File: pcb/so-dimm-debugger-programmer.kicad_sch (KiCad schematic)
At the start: 22 parts, among them J1 1612618-4, J12 Conn_01x06_Pin, J2 Conn_01x06_Pin, J3 Conn_01x04_Pin, J4 Conn_01x04_Pin, J8 Conn_02x16_Odd_Even, J9 Conn_01x04_Pin, SW1 SW_Push, SW2 SW_Push, U1 AP2112K-3.3

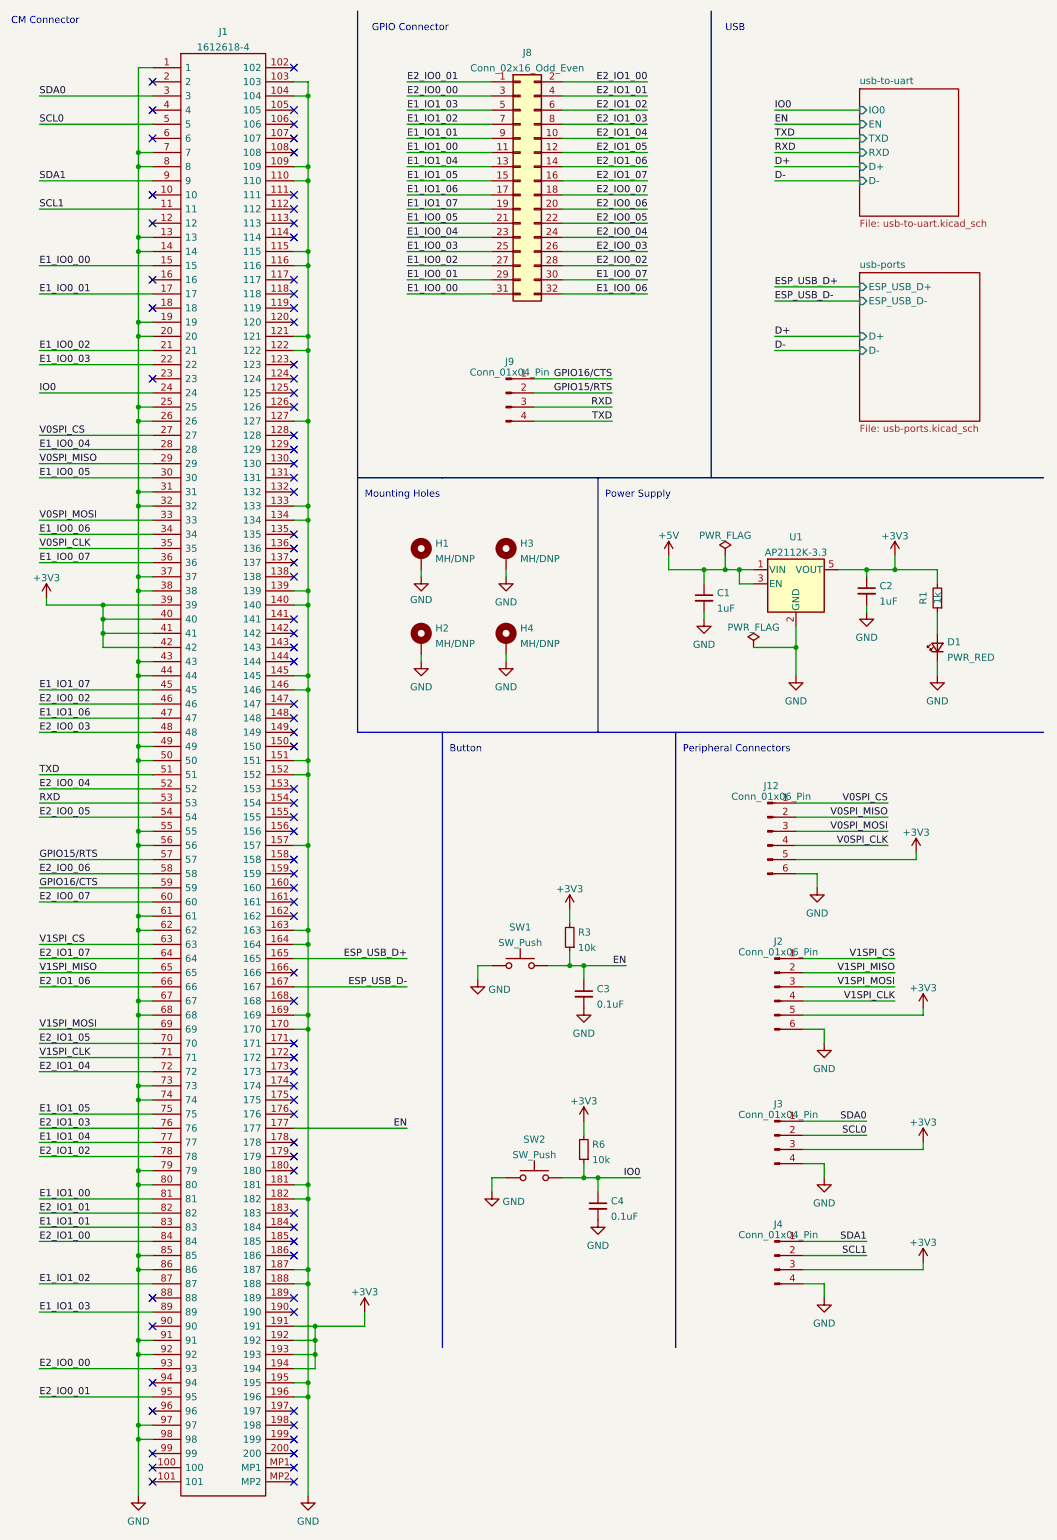
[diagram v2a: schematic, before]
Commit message: Fixed Rx Tx not being swapped between CP2102 and ESP-CM3 connector
+ Fix Label for PWR and Rx (swapped)
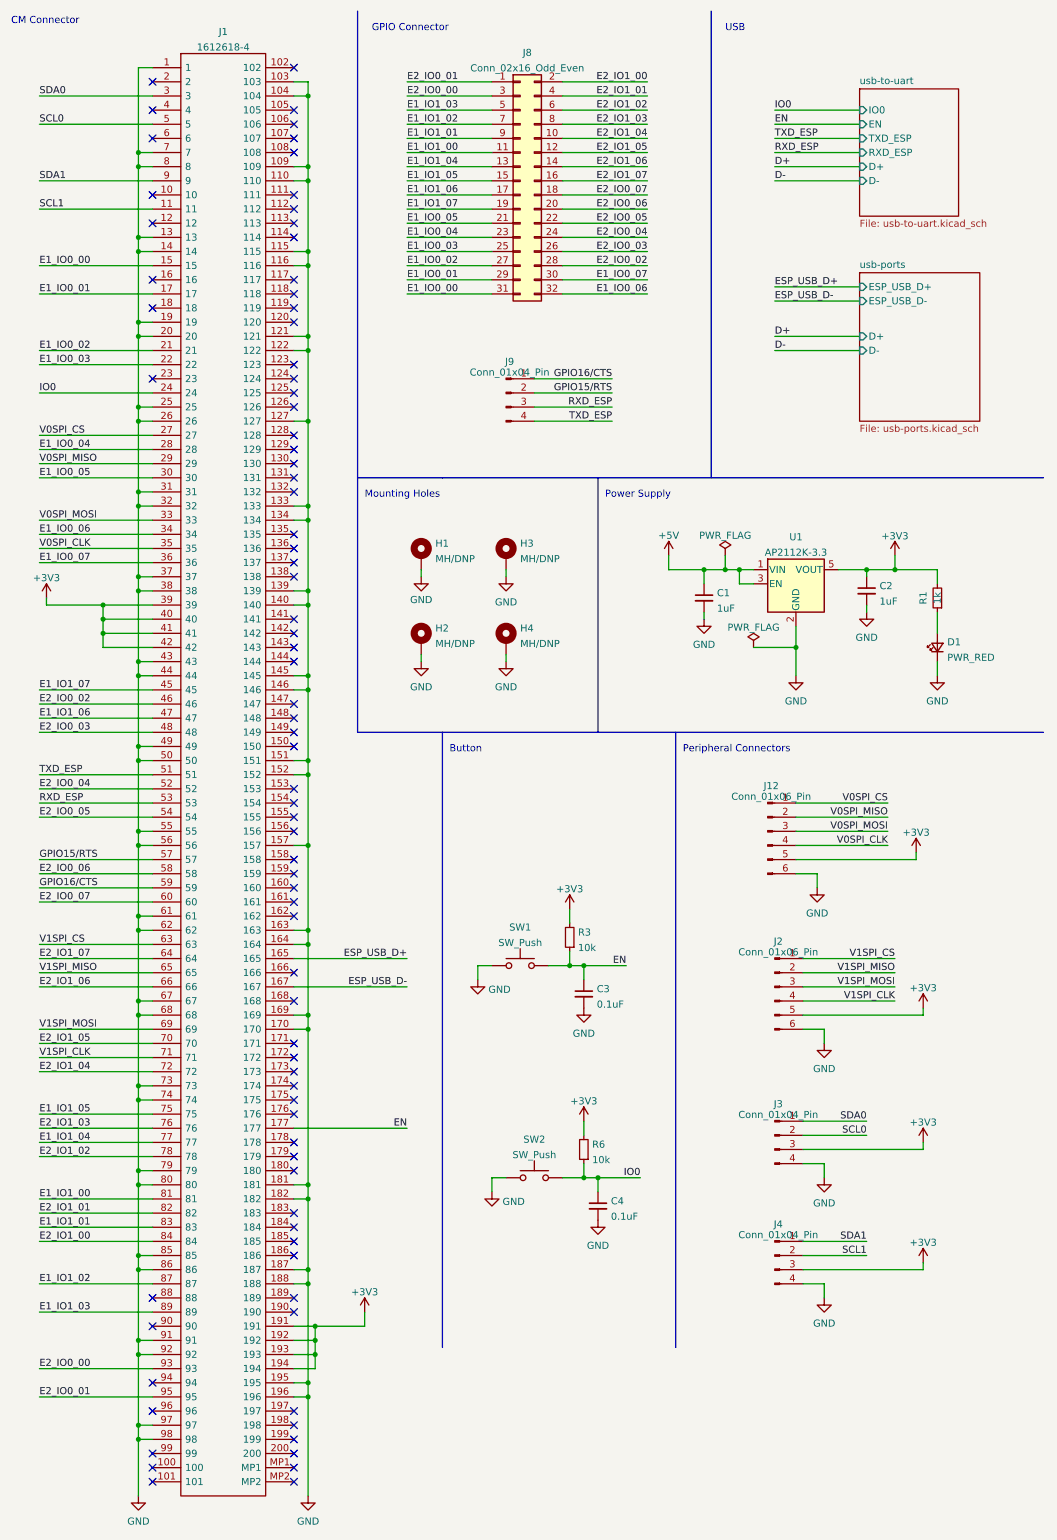
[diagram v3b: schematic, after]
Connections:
- net RXD renamed RXD_ESP
- net TXD renamed TXD_ESP
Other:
- sheet usb-to-uart ports: added RXD_ESP, TXD_ESP; removed RXD, TXD
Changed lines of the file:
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@@
     (effects (font (size 1.27 1.27)) (justify left bottom))
+  )
+  (label "TXD_ESP" (at 120.65 86.36 180) (fields_autoplaced)
+    (effects (font (size 1.27 1.27)) (justify right bottom))
   )
   (label "E2_IO0_00" (at 17.78 256.54 0) (fields_autoplaced)
@@
     (effects (font (size 1.27 1.27)) (justify left bottom))
   )
-  (label "TXD" (at 17.78 149.86 0) (fields_autoplaced)
-    (effects (font (size 1.27 1.27)) (justify left bottom))
-  )
   (label "E2_IO1_07" (at 17.78 182.88 0) (fields_autoplaced)
     (effects (font (size 1.27 1.27)) (justify left bottom))
@@
     (effects (font (size 1.27 1.27)) (justify right bottom))
   )
+  (label "TXD_ESP" (at 17.78 149.86 0) (fields_autoplaced)
+    (effects (font (size 1.27 1.27)) (justify left bottom))
+  )
   (label "D-" (at 149.86 43.18 0) (fields_autoplaced)
     (effects (font (size 1.27 1.27)) (justify left bottom))
@@
     (effects (font (size 1.27 1.27)) (justify left bottom))
   )
+  (label "RXD_ESP" (at 120.65 83.82 180) (fields_autoplaced)
+    (effects (font (size 1.27 1.27)) (justify right bottom))
+  )
   (label "E2_IO1_01" (at 127 27.94 180) (fields_autoplaced)
     (effects (font (size 1.27 1.27)) (justify right bottom))
   )
-  (label "TXD" (at 149.86 35.56 0) (fields_autoplaced)
+  (label "TXD_ESP" (at 149.86 35.56 0) (fields_autoplaced)
     (effects (font (size 1.27 1.27)) (justify left bottom))
   )
@@
     (effects (font (size 1.27 1.27)) (justify left bottom))
   )
-  (label "RXD" (at 120.65 83.82 180) (fields_autoplaced)
-    (effects (font (size 1.27 1.27)) (justify right bottom))
-  )
   (label "EN" (at 83.82 213.36 180) (fields_autoplaced)
     (effects (font (size 1.27 1.27)) (justify right bottom))
   )
-  (label "RXD" (at 17.78 154.94 0) (fields_autoplaced)
-    (effects (font (size 1.27 1.27)) (justify left bottom))
-  )
   (label "SDA1" (at 166.37 233.68 180) (fields_autoplaced)
     (effects (font (size 1.27 1.27)) (justify right bottom))
@@
     (effects (font (size 1.27 1.27)) (justify left bottom))
   )
-  (label "RXD" (at 149.86 38.1 0) (fields_autoplaced)
+  (label "RXD_ESP" (at 149.86 38.1 0) (fields_autoplaced)
     (effects (font (size 1.27 1.27)) (justify left bottom))
   )
@@
     (effects (font (size 1.27 1.27)) (justify right bottom))
   )
+  (label "RXD_ESP" (at 17.78 154.94 0) (fields_autoplaced)
+    (effects (font (size 1.27 1.27)) (justify left bottom))
+  )
   (label "E1_IO0_06" (at 17.78 106.68 0) (fields_autoplaced)
     (effects (font (size 1.27 1.27)) (justify left bottom))
@@
   (label "E2_IO0_05" (at 17.78 157.48 0) (fields_autoplaced)
     (effects (font (size 1.27 1.27)) (justify left bottom))
-  )
-  (label "TXD" (at 120.65 86.36 180) (fields_autoplaced)
-    (effects (font (size 1.27 1.27)) (justify right bottom))
   )
   (label "V0SPI_MISO" (at 170.18 157.48 180) (fields_autoplaced)
@@
       (effects (font (size 1.27 1.27)) (justify left))
     )
-    (pin "TXD" input (at 165.1 35.56 180)
-      (effects (font (size 1.27 1.27)) (justify left))
-    )
-    (pin "RXD" input (at 165.1 38.1 180)
-      (effects (font (size 1.27 1.27)) (justify left))
-    )
     (pin "D+" input (at 165.1 40.64 180)
       (effects (font (size 1.27 1.27)) (justify left))
@@
       (effects (font (size 1.27 1.27)) (justify left))
     )
+    (pin "TXD_ESP" input (at 165.1 35.56 180)
+      (effects (font (size 1.27 1.27)) (justify left))
+    )
+    (pin "RXD_ESP" input (at 165.1 38.1 180)
+      (effects (font (size 1.27 1.27)) (justify left))
+    )

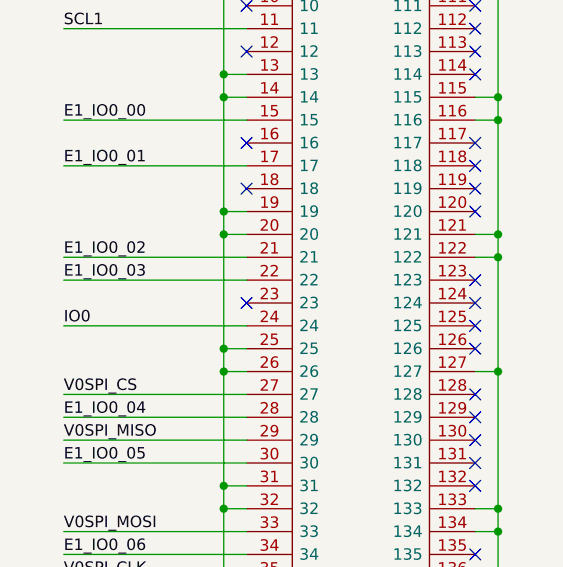
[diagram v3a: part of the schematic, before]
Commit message: Fix E1_IO0_3 connected to Pin 22 instead of 23
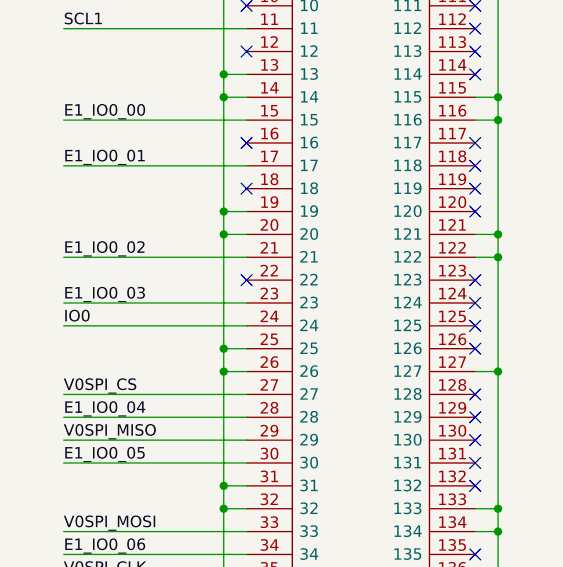
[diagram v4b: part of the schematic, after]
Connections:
- net E1_IO0_03: now also J1.23; no longer J1.22
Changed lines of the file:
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@@
   (no_connect (at 63.5 78.74))
   (no_connect (at 63.5 76.2))
-  (no_connect (at 38.1 78.74))
   (no_connect (at 63.5 129.54))
   (no_connect (at 63.5 127))
@@
   (no_connect (at 63.5 215.9))
   (no_connect (at 63.5 210.82))
+  (no_connect (at 38.1 76.2))
   (no_connect (at 38.1 264.16))
   (no_connect (at 38.1 259.08))
@@
     (stroke (width 0) (type default))
   )
-  (wire (pts (xy 17.78 76.2) (xy 38.1 76.2))
+  (wire (pts (xy 17.78 78.74) (xy 38.1 78.74))
     (stroke (width 0) (type default))
   )
@@
     (effects (font (size 1.27 1.27)) (justify right bottom))
   )
-  (label "E1_IO0_03" (at 17.78 76.2 0) (fields_autoplaced)
-    (effects (font (size 1.27 1.27)) (justify left bottom))
-  )
+  (label "E1_IO0_03" (at 17.78 78.74 0) (fields_autoplaced)
+    (effects (font (size 1.27 1.27)) (justify left bottom))
+  )

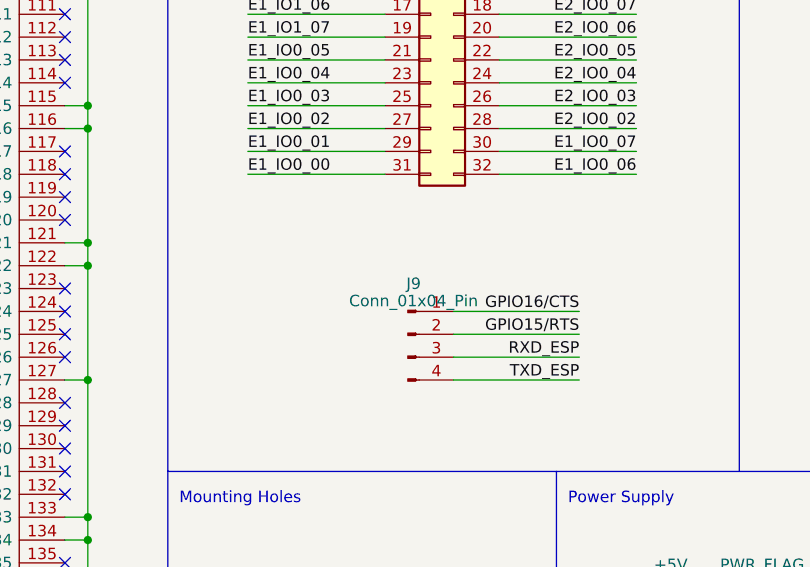
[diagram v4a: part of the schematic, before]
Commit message: Removed unpopulated pin header from BOM
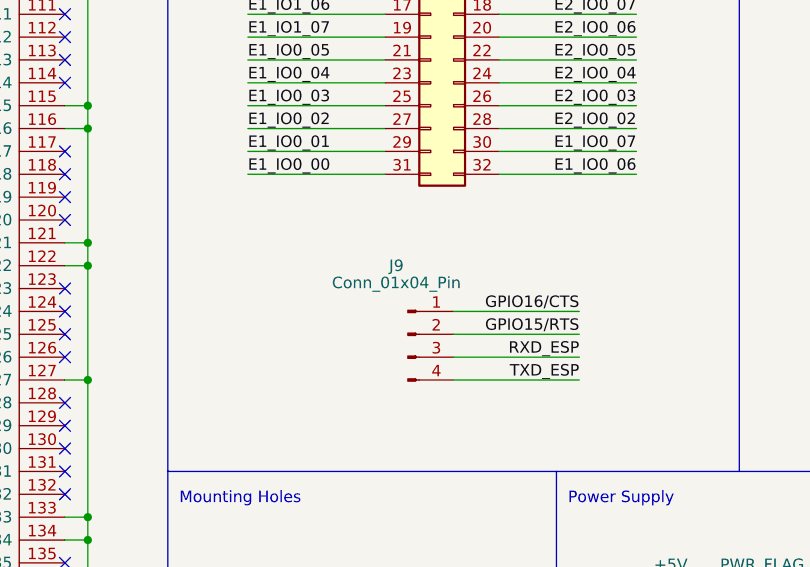
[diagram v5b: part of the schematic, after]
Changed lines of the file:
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@@
   )
   (symbol (lib_id "Connector:Conn_01x04_Pin") (at 101.6 81.28 0) (unit 1)
-    (in_bom yes) (on_board yes) (dnp no) (fields_autoplaced)
-    (property "Reference" "J9" (at 102.235 75.6539 0)
+    (in_bom yes) (on_board yes) (dnp no)
+    (property "Reference" "J9" (at 100.33 73.66 0)
       (effects (font (size 1.27 1.27)))
     )
-    (property "Value" "Conn_01x04_Pin" (at 102.235 77.5749 0)
+    (property "Value" "Conn_01x04_Pin" (at 100.33 75.565 0)
       (effects (font (size 1.27 1.27)))
     )

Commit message: Added date and revision to schematic
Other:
- company: (none) -> OPEN THINGS
- title: (none) -> ESP-CM3 Programmer
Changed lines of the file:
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@@
   (paper "A4" portrait)
   (title_block
-    (date "2022-11-02")
+    (title "ESP-CM3 Programmer")
+    (date "2023-09-29")
+    (rev "REV.01")
+    (company "OPEN THINGS")
   )
   (junction (at 35.56 83.82) (diameter 0) (color 0 0 0 0)

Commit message: Added generated data
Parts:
- H1, H2, H3, H4: now left out of the parts list
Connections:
- net E1_IO0_00: now also J8.32 (Pin_32); no longer J8.31 (Pin_31)
- net E1_IO0_01: now also J8.30 (Pin_30); no longer J8.29 (Pin_29)
- net E1_IO0_02: now also J8.28 (Pin_28); no longer J8.27 (Pin_27)
- net E1_IO0_03: now also J8.26 (Pin_26); no longer J8.25 (Pin_25)
- net E1_IO0_04: now also J8.24 (Pin_24); no longer J8.23 (Pin_23)
- net E1_IO0_05: now also J8.22 (Pin_22); no longer J8.21 (Pin_21)
- net E1_IO0_06: now also J8.31 (Pin_31); no longer J8.32 (Pin_32)
- net E1_IO0_07: now also J8.29 (Pin_29); no longer J8.30 (Pin_30)
- net E1_IO1_00: now also J8.12 (Pin_12); no longer J8.11 (Pin_11)
- net E1_IO1_01: now also J8.10 (Pin_10); no longer J8.9 (Pin_9)
- net E1_IO1_02: now also J8.8 (Pin_8); no longer J8.7 (Pin_7)
- net E1_IO1_03: now also J8.6 (Pin_6); no longer J8.5 (Pin_5)
- net E1_IO1_04: now also J8.14 (Pin_14); no longer J8.13 (Pin_13)
- net E1_IO1_05: now also J8.16 (Pin_16); no longer J8.15 (Pin_15)
- net E1_IO1_06: now also J8.18 (Pin_18); no longer J8.17 (Pin_17)
- net E1_IO1_07: now also J8.20 (Pin_20); no longer J8.19 (Pin_19)
- net E2_IO0_00: now also J8.4 (Pin_4); no longer J8.3 (Pin_3)
- net E2_IO0_01: now also J8.2 (Pin_2); no longer J8.1 (Pin_1)
- net E2_IO0_02: now also J8.27 (Pin_27); no longer J8.28 (Pin_28)
- net E2_IO0_03: now also J8.25 (Pin_25); no longer J8.26 (Pin_26)
- net E2_IO0_04: now also J8.23 (Pin_23); no longer J8.24 (Pin_24)
- net E2_IO0_05: now also J8.21 (Pin_21); no longer J8.22 (Pin_22)
- net E2_IO0_06: now also J8.19 (Pin_19); no longer J8.20 (Pin_20)
- net E2_IO0_07: now also J8.17 (Pin_17); no longer J8.18 (Pin_18)
- net E2_IO1_00: now also J8.1 (Pin_1); no longer J8.2 (Pin_2)
- net E2_IO1_01: now also J8.3 (Pin_3); no longer J8.4 (Pin_4)
- net E2_IO1_02: now also J8.5 (Pin_5); no longer J8.6 (Pin_6)
- net E2_IO1_03: now also J8.7 (Pin_7); no longer J8.8 (Pin_8)
- net E2_IO1_04: now also J8.9 (Pin_9); no longer J8.10 (Pin_10)
- net E2_IO1_05: now also J8.11 (Pin_11); no longer J8.12 (Pin_12)
- net E2_IO1_06: now also J8.13 (Pin_13); no longer J8.14 (Pin_14)
- net E2_IO1_07: now also J8.15 (Pin_15); no longer J8.16 (Pin_16)
- net GND: no longer H1.1, H2.1, H3.1, H4.1
- no-connect marks 81 -> 85
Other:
- title: ESP-CM3 Programmer -> ESP-CM3-Programmer
